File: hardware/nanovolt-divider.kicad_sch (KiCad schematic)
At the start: 12 parts, among them J1 NORMAL IN +, J2 NORMAL IN -, J3 HV IN +, J4 HV IN -, J5 DIVIDER OUT HI, J6 DIVIDER OUT LO, SW1 SW_3PDT NORMAL/HV

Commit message: PCB: placed, unrouted Rev0 board with HV rules and project footprints
- hardware/nanovolt-divider.kicad_pcb: 100 x 62 mm, 2 layers, control /
  precision sections separated by a slot, relays in a row across from
  their drivers, HV parts spaced, 1 ohm corner with L slot and TMP117,
  GND pour limited to the control section, precision no-pour keepout,
  4x M3 holes. Nets assigned from the schematic netlist; no tracks yet.
- hardware/nanovolt-divider.kicad_dru: HV netclass clearance 3 mm,
  creepage 4 mm, edge clearance; DSBGA clearance; slot-bridge track width
- Project footprints authored from datasheets / measured parts: Ohmite
  MOX-700, Slim-Mox SM102, Vishay RS-2C, 3x3 switch wiring pads
- Schematic: footprints assigned, HV netclass in project, SW1 on wire pads
- tools/gen_pcb.py: bootstrap board generator (placement + DRC via kicad-cli)
- DRC: only unrouted ratsnest and silkscreen-over-pad warnings remain

Co-Authored-By: Claude Fable 5.1 <noreply@anthropic.com>
Claude-Session: https://claude.ai/code/session_012iVAGTG9sDDBFakz9fB6fg
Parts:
- R31, R32: footprint Resistor_THT:R_Axial_DIN0207_L6.3mm_D2.5mm_P10.16mm_Horizontal -> nanovolt-divider:R_Axial_Ohmite_MOX700_L7.0mm_D2.7mm_P10.16mm_Horizontal
- R33, R34: footprint Resistor_THT:R_Box_L14.0mm_W5.0mm_P9.00mm -> nanovolt-divider:R_Radial_Ohmite_SlimMox_SM102_L14.7mm_W2.5mm_P10.16mm
- R35: footprint Resistor_THT:R_Axial_DIN0411_L9.9mm_D3.6mm_P12.70mm_Horizontal -> nanovolt-divider:R_Axial_Vishay_RS02C_L15.1mm_D5.6mm_P20.32mm_Horizontal
- SW1: footprint TerminalBlock_Phoenix:TerminalBlock_Phoenix_MKDS-3-9-5.08_1x09_P5.08mm_Horizontal -> nanovolt-divider:SW_3PDT_WirePads_3x3_P7.62mm

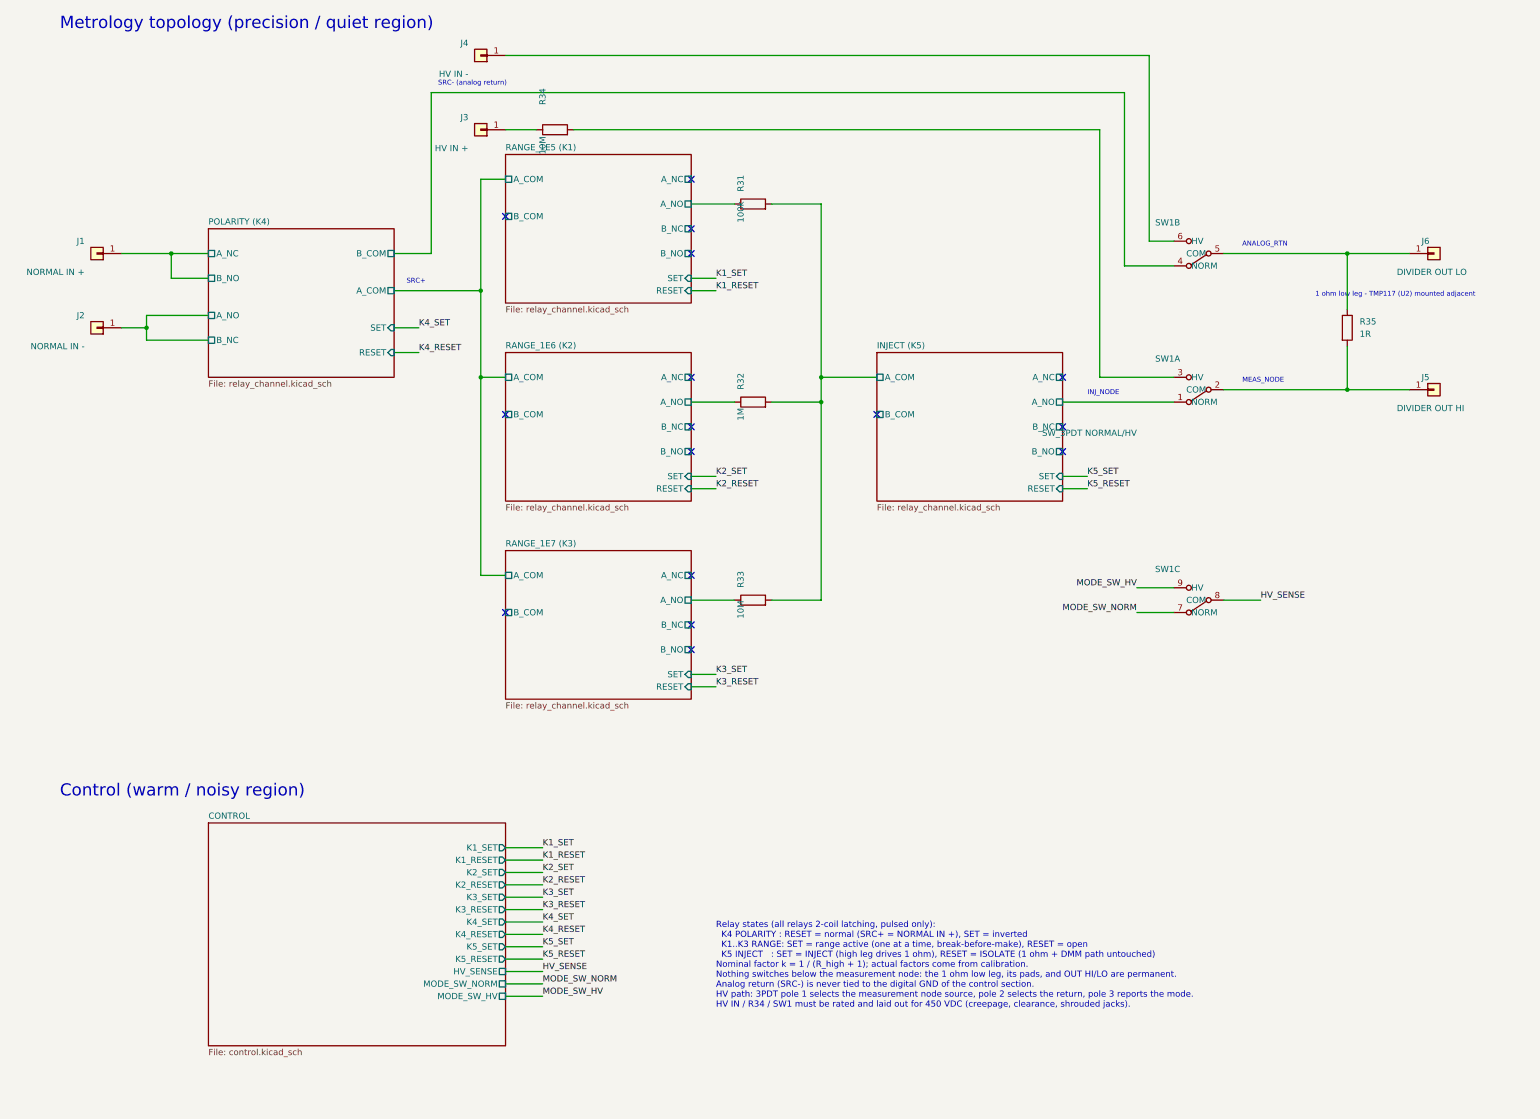
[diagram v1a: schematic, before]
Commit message: Rev0: named analog nets, both relay poles, HV netclass, smaller board
Restore the HV netclass (the real bug)
--------------------------------------
nanovolt-divider.kicad_dru conditions all three 450 V rules on NetClass == 'HV',
but the project file had "netclass_patterns": [] and no HV class, so every one of
them matched nothing. DRC reported "0 violations" whether the board was safe or
not. The original patterns matched auto-generated names like Net-(J3-Pin_1) and
were dropped when KiCad rewrote the project file.

The class is back with the patterns spelled out - /HV_IN_P and /HV_DIV, never a
"HV*" wildcard, which would sweep in HV_SENSE (a 3.3 V logic line). Verified by
moving R34 next to K5 on a scratch copy and confirming the rules fire; restoring
them immediately exposed 25 real clearance/creepage violations in the old
placement, now fixed.

gen_schematics.py no longer overwrites .kicad_pro (write_once): it emits a
25-line stub, and KiCad owns the 702-line file that holds the netclass.

Schematic
---------
* Analog nets carry real labels instead of /POLARITY (K4)/A_COM and
  Net-(J4-Pin_1): SRC_P, SRC_RTN, NORMAL_IN_P/N, RANGE_BUS, R*_IN, R*_OUT,
  INJ_NODE, MEAS_NODE, ANALOG_RTN, HV_IN_P, HV_DIV. This is also what gives the
  HV netclass stable patterns to match.
* K1..K3 use both poles: SRC_P -> A_COM -> A_NO -> R -> B_NO -> B_COM ->
  RANGE_BUS, so a deselected high leg is isolated at both ends.
* Control ground is DGND, not the global GND, so it cannot merge with the
  floating analog return.
* J7/J8/J9 use project symbols with the module's own pin names (SCL_IO22, IO35)
  instead of Conn_01x04 Pin_1..Pin_4. Pin geometry is unchanged, so no wire moved.
* Removed from the board: J4 (HV IN- is a panel-to-panel wire to SW1 lug 6), R26
  and SW1 lug 7 (R25's 100k already holds HV_SENSE low off the HV throw). Added
  C5 10 nF to stiffen the 100k against pickup on the IO35 harness. The two
  off-board lugs are documented in a panel-wiring note on the root sheet.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
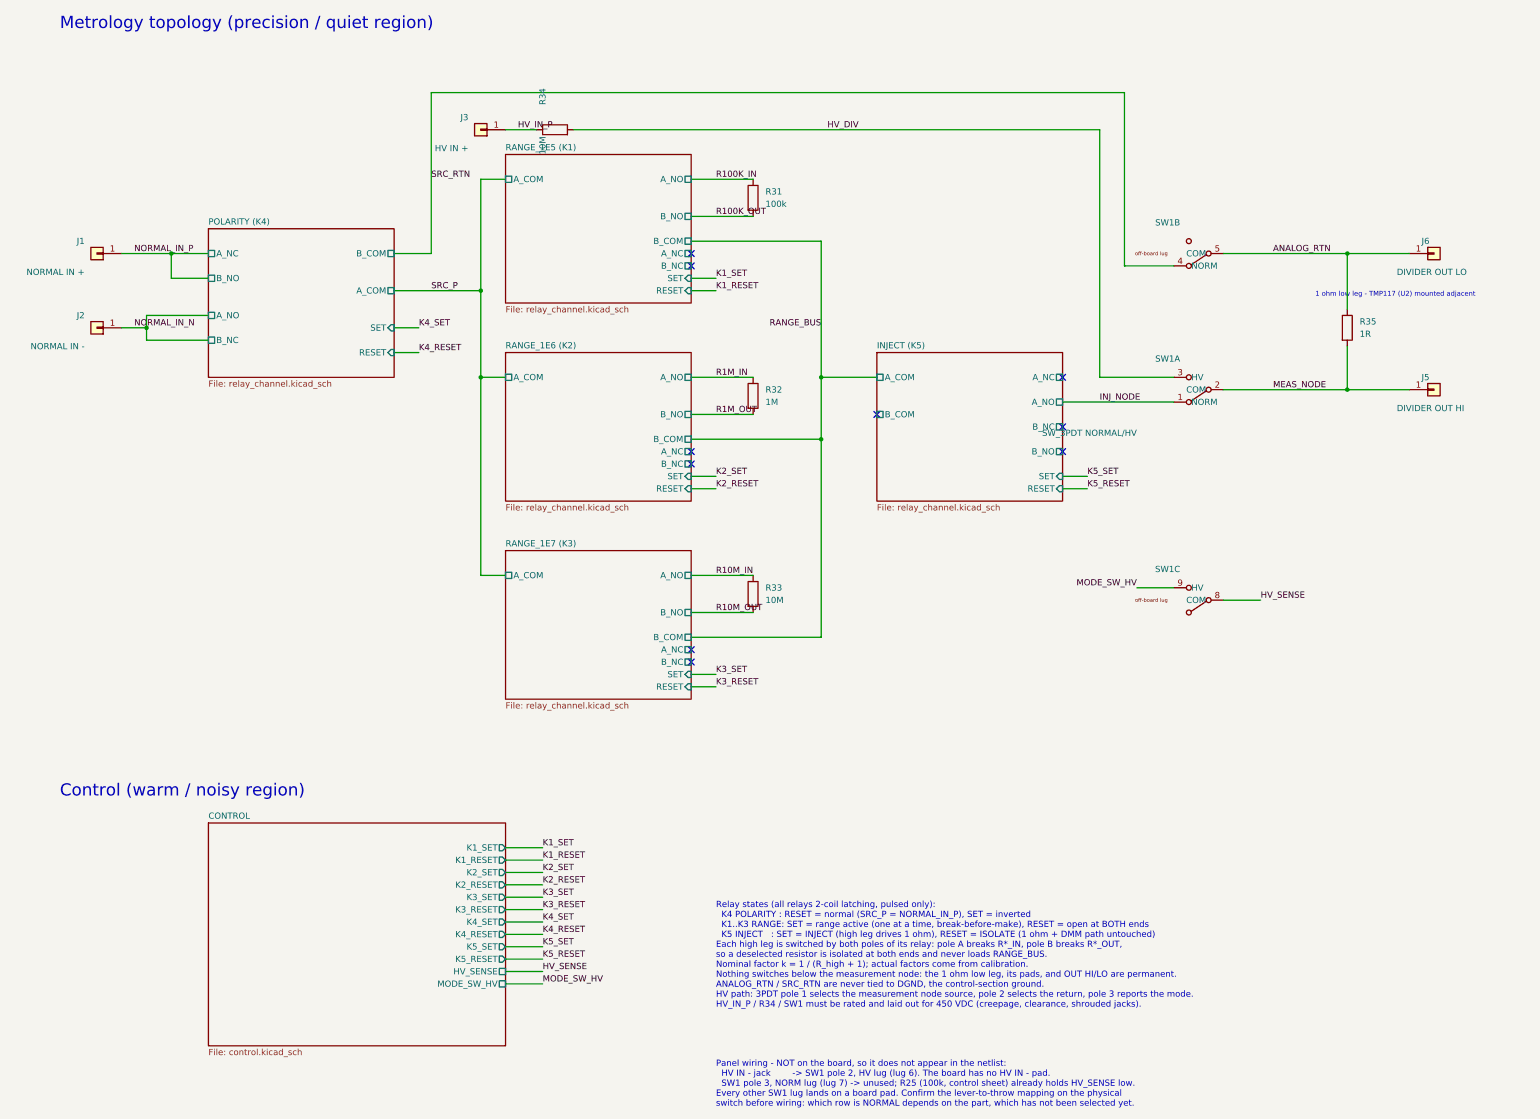
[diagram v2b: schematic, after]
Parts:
- removed J4: HV IN -, Connector_Wire:SolderWire-0.25sqmm_1x01_D0.65mm_OD1.7mm, symbol Connector_Generic:Conn_01x01
- SW1: footprint nanovolt-divider:SW_3PDT_WirePads_3x3_P7.62mm -> nanovolt-divider:SW_3PDT_WirePads_Split
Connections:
- net HV_IN_P: now reaches J3.1 (Pin_1), R34.1
- net ANALOG_RTN: now reaches J6.1 (Pin_1), R35.1, SW1.5 (COM)
- net MEAS_NODE: now reaches J5.1 (Pin_1), R35.2, SW1.2 (COM)
- net HV_DIV: now reaches R34.2, SW1.3 (HV)
- removed net INJECT (K5)/A_COM: R31.2, R32.2, R33.2
- net INJECT (K5)/A_NO renamed INJ_NODE
- removed net MODE_SW_NORM: SW1.7 (NORM)
- net POLARITY (K4)/A_NC renamed NORMAL_IN_P
- net POLARITY (K4)/A_NO renamed NORMAL_IN_N
- net POLARITY (K4)/B_COM renamed SRC_RTN
- net RANGE_1E5 (K1)/A_NO renamed R100K_IN
- net RANGE_1E6 (K2)/A_NO renamed R1M_IN
- net RANGE_1E7 (K3)/A_NO renamed R10M_IN
- new net R100K_OUT: R31.2
- new net R10M_OUT: R33.2
- new net R1M_OUT: R32.2
- no-connect marks 16 -> 10
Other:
- sheet CONTROL ports: added none; removed MODE_SW_NORM
- note added: "Panel wiring - NOT on the board, so it does not appear in the netlist: HV IN - jack -> SW1 pole 2, HV lug (lug 6). The board has no HV IN - pad. SW1 pole 3, NORM lug (lug 7) -> unused; R25 (100k, control sheet) already holds HV_SENSE low. Every other SW1 lug lands on a board pad. Confirm the lever-to-throw mapping on the physical switch before wiring: which row is NORMAL depends on the part, whic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"
- note added: "Relay states (all relays 2-coil latching, pulsed only): K4 POLARITY : RESET = normal (SRC_P = NORMAL_IN_P), SET = inverted K1..K3 RANGE: SET = range active (one at a time, break-before-make), RESET = open at BOTH ends K5 INJECT : SET = INJECT (high leg drives 1 ohm), RESET = ISOLATE (1 ohm + DMM path untouched) Each high leg is switched by both poles of its relay: pole A breaks R*_IN, pole B brea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"
- note removed: "ANALOG_RTN"
- note removed: "INJ_NODE"
- note removed: "MEAS_NODE"
- note removed: "Relay states (all relays 2-coil latching, pulsed only): K4 POLARITY : RESET = normal (SRC+ = NORMAL IN +), SET = inverted K1..K3 RANGE: SET = range active (one at a time, break-before-make), RESET = open K5 INJECT : SET = INJECT (high leg drives 1 ohm), RESET = ISOLATE (1 ohm + DMM path untouched) Nominal factor k = 1 / (R_high + 1); actual factors come from calibration. Nothing switches below th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"
- note removed: "SRC+"
- note removed: "SRC- (analog return)"
- moved on the sheet: R31

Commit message: K5 pole B breaks the return leg: ISOLATE now opens both sides
Pole A already broke the high side (RANGE_BUS -> INJ_NODE); pole B was unused
with all three pins no-connect. It now breaks the return in step with it:
SRC_RTN -> K5 B_COM, K5 B_NO -> INJ_RTN -> 3PDT pole 2 NORMAL throw.

In ISOLATE the programmable source is now detached from the 1 ohm and the DMM
path at both ends, so none of it - output capacitance, cabling, leakage to earth
- stays attached to the measurement node.

SRC_RTN and INJ_RTN are carried by net label rather than a polyline: a drawn wire
from K5 pole B across to the switch would have to cross both INJ_NODE and HV_DIV.

Net changes: /SRC_RTN is now K4.8 + K5.8 (was K4.8 + SW1.4); /INJ_RTN is new
(K5.7 + SW1.4). K5 A_NC and B_NC remain no-connect. Nothing else moved.

ERC 0, DRC 0 errors, 0 schematic-parity issues; HV netclass intact.

Co-Authored-By: Claude Opus 5 <noreply@anthropic.com>
Claude-Session: https://claude.ai/code/session_0168vwTBRM7XaQRxDqmVSFLB
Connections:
- net SRC_RTN: no longer SW1.4 (NORM)
- new net INJ_RTN: SW1.4 (NORM)
- no-connect marks 10 -> 8
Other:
- note added: "Relay states (all relays 2-coil latching, pulsed only): K4 POLARITY : RESET = normal (SRC_P = NORMAL_IN_P), SET = inverted K1..K3 RANGE: SET = range active (one at a time, break-before-make), RESET = open at BOTH ends K5 INJECT : SET = INJECT (high leg drives 1 ohm), RESET = ISOLATE - both legs open, the source is disconnected from the 1 ohm and the DMM path at both ends Each high leg is switched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"
- note removed: "Relay states (all relays 2-coil latching, pulsed only): K4 POLARITY : RESET = normal (SRC_P = NORMAL_IN_P), SET = inverted K1..K3 RANGE: SET = range active (one at a time, break-before-make), RESET = open at BOTH ends K5 INJECT : SET = INJECT (high leg drives 1 ohm), RESET = ISOLATE (1 ohm + DMM path untouched) Each high leg is switched by both poles of its relay: pole A breaks R*_IN, pole B brea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"
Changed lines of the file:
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@@
 	  (instances (project "nanovolt-divider" (path "/6b173215-4dcb-58a2-8716-bf25a1870e1e" (page "7"))))
 	)
-	(no_connect (at 193.04 93.98))
+	(wire (pts (xy 185.42 93.98) (xy 193.04 93.98)) (stroke (width 0) (type default)))
+	(label "SRC_RTN" (at 185.42 93.98 180) (effects (font (size 1.27 1.27)) (justify right bottom)))
+	(wire (pts (xy 231.14 101.6) (xy 238.76 101.6)) (stroke (width 0) (type default)))
+	(label "INJ_RTN" (at 238.76 101.6 0) (effects (font (size 1.27 1.27)) (justify left bottom)))
 	(no_connect (at 231.14 86.36))
 	(no_connect (at 231.14 96.52))
-	(no_connect (at 231.14 101.6))
 	(wire (pts (xy 231.14 106.68) (xy 236.22 106.68)) (stroke (width 0) (type default)))
 	(label "K5_SET" (at 236.22 106.68 0) (effects (font (size 1.27 1.27)) (justify left bottom)))
@@
 	(label "INJ_NODE" (at 238.76 91.44 0) (effects (font (size 1.27 1.27)) (justify left bottom)))
 	(wire (pts (xy 93.98 60.96) (xy 101.6 60.96)) (stroke (width 0) (type default)))
-	(wire (pts (xy 101.6 60.96) (xy 101.6 27.94)) (stroke (width 0) (type default)))
-	(wire (pts (xy 101.6 27.94) (xy 243.84 27.94)) (stroke (width 0) (type default)))
-	(wire (pts (xy 243.84 27.94) (xy 243.84 63.5)) (stroke (width 0) (type default)))
-	(wire (pts (xy 243.84 63.5) (xy 254 63.5)) (stroke (width 0) (type default)))
-	(label "SRC_RTN" (at 101.6 45.72 0) (effects (font (size 1.27 1.27)) (justify left bottom)))
+	(label "SRC_RTN" (at 101.6 60.96 0) (effects (font (size 1.27 1.27)) (justify left bottom)))
+	(wire (pts (xy 246.38 63.5) (xy 254 63.5)) (stroke (width 0) (type default)))
+	(label "INJ_RTN" (at 246.38 63.5 180) (effects (font (size 1.27 1.27)) (justify right bottom)))
 	(wire (pts (xy 254 129.54) (xy 246.38 129.54)) (stroke (width 0) (type default)))
 	(label "MODE_SW_HV" (at 246.38 129.54 180) (effects (font (size 1.27 1.27)) (justify right bottom)))
@@
 	(text "Metrology topology (precision / quiet region)" (at 25.4 15.24 0) (effects (font (size 2.5 2.5)) (justify left bottom)))
 	(text "Control (warm / noisy region)" (at 25.4 172.72 0) (effects (font (size 2.5 2.5)) (justify left bottom)))
-	(text "Relay states (all relays 2-coil latching, pulsed only):\n  K4 POLARITY : RESET = normal (SRC_P = NORMAL_IN_P), SET = inverted\n  K1..K3 RANGE: SET = range active (one at a time, break-before-make), RESET = open at BOTH ends\n  K5 INJECT   : SET = INJECT (high leg drives 1 ohm), RESET = ISOLATE (1 ohm + DMM path untouched)\nEach high leg is switched by both poles of its relay: pole A breaks R*_IN, pole B breaks R*_OUT,\nso a deselected resistor is isolated at both ends and never loads RANGE_BUS.\nNominal factor k = 1 / (R_high + 1); actual factors come from calibration.\nNothing switches below the measurement node: the 1 ohm low leg, its pads, and OUT HI/LO are permanent.\nANALOG_RTN / SRC_RTN are never tied to DGND, the control-section ground.\nHV path: 3PDT pole 1 selects the measurement node source, pole 2 selects the return, pole 3 reports the mode.\nHV_IN_P / R34 / SW1 must be rated and laid out for 450 VDC (creepage, clearance, shrouded jacks)." (at 160.02 215.9 0) (effects (font (size 1.27 1.27)) (justify left bottom)))
+	(text "Relay states (all relays 2-coil latching, pulsed only):\n  K4 POLARITY : RESET = normal (SRC_P = NORMAL_IN_P), SET = inverted\n  K1..K3 RANGE: SET = range active (one at a time, break-before-make), RESET = open at BOTH ends\n  K5 INJECT   : SET = INJECT (high leg drives 1 ohm), RESET = ISOLATE - both legs open,\n                the source is disconnected from the 1 ohm and the DMM path at both ends\nEach high leg is switched by both poles of its relay: pole A breaks R*_IN, pole B breaks R*_OUT,\nso a deselected resistor is isolated at both ends and never loads RANGE_BUS.\nNominal factor k = 1 / (R_high + 1); actual factors come from calibration.\nNothing switches below the measurement node: the 1 ohm low leg, its pads, and OUT HI/LO are permanent.\nANALOG_RTN / SRC_RTN are never tied to DGND, the control-section ground.\nHV path: 3PDT pole 1 selects the measurement node source, pole 2 selects the return, pole 3 reports the mode.\nHV_IN_P / R34 / SW1 must be rated and laid out for 450 VDC (creepage, clearance, shrouded jacks)." (at 160.02 215.9 0) (effects (font (size 1.27 1.27)) (justify left bottom)))
 	(text "Panel wiring - NOT on the board, so it does not appear in the netlist:\n  HV IN - jack        -> SW1 pole 2, HV lug (lug 6). The board has no HV IN - pad.\n  SW1 pole 3, NORM lug (lug 7) -> unused; R25 (100k, control sheet) already holds HV_SENSE low.\nEvery other SW1 lug lands on a board pad. Confirm the lever-to-throw mapping on the physical\nswitch before wiring: which row is NORMAL depends on the part, which has not been selected yet." (at 160.02 236.22 0) (effects (font (size 1.27 1.27)) (justify left bottom)))
 	(text "1 ohm low leg - TMP117 (U2) mounted adjacent" (at 283 70 0) (effects (font (size 1.0 1.0)) (justify left bottom)))
